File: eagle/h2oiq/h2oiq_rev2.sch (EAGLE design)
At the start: 25 parts, among them T1 Darlington, T2 BC846

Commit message: Minor board change for the LPFK
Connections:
- net SERVOON: now also ATMEL.PD2(INT0/PCINT18)
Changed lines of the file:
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@@
 <label x="33.02" y="27.94" size="1.778" layer="95"/>
+</segment>
+<segment>
+<pinref part="ATMEL" gate="1" pin="PD2(INT0/PCINT18)"/>
+<wire x1="25.4" y1="83.82" x2="30.48" y2="83.82" width="0.1524" layer="91"/>
+<label x="33.02" y="83.82" size="1.778" layer="95"/>
 </segment>
 </net>

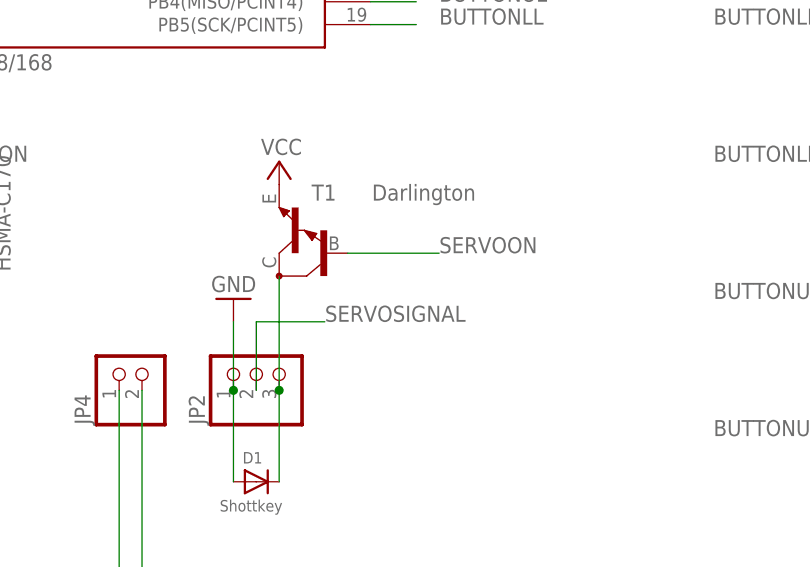
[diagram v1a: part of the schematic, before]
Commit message: Adding Demo Arduino Code, as well as updated board changes
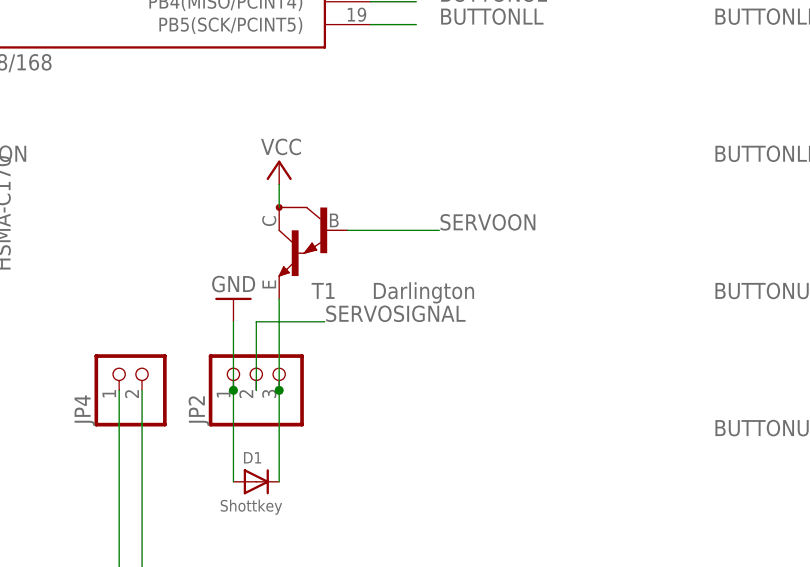
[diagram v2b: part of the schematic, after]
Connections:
- net SERVOACT: now also T1.E; no longer T1.C
- net VCC: now also T1.C; no longer T1.E
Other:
- moved on the sheet: T1
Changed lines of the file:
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@@
 <attribute name="VALUE" x="8.636" y="0.508" size="1.27" layer="96" rot="MR180"/>
 </instance>
-<instance part="T1" gate="G$1" x="20.32" y="27.94" smashed="yes" rot="R180">
-<attribute name="NAME" x="21.59" y="35.56" size="1.778" layer="95" rot="R180"/>
-<attribute name="VALUE" x="37.084" y="35.56" size="1.778" layer="96" rot="R180"/>
+<instance part="T1" gate="G$1" x="20.32" y="30.48" smashed="yes" rot="MR0">
+<attribute name="NAME" x="21.59" y="22.86" size="1.778" layer="95" rot="MR0"/>
+<attribute name="VALUE" x="37.084" y="22.86" size="1.778" layer="96" rot="MR0"/>
 </instance>
 <instance part="LED1" gate="G$1" x="-20.32" y="25.4"/>
@@
 </segment>
 <segment>
-<pinref part="P+6" gate="VCC" pin="VCC"/>
-<pinref part="T1" gate="G$1" pin="E"/>
-</segment>
-<segment>
 <pinref part="XBEE" gate="G$1" pin="VCC"/>
 <pinref part="P+3" gate="VCC" pin="VCC"/>
@@
 <label x="10.16" y="-15.24" size="1.778" layer="95"/>
 <pinref part="JP4" gate="G$1" pin="2"/>
+</segment>
+<segment>
+<pinref part="T1" gate="G$1" pin="C"/>
+<pinref part="P+6" gate="VCC" pin="VCC"/>
+<wire x1="15.24" y1="33.02" x2="15.24" y2="35.56" width="0.1524" layer="91"/>
 </segment>
 </net>
@@
 <net name="SERVOACT" class="0">
 <segment>
-<pinref part="T1" gate="G$1" pin="C"/>
-<wire x1="15.24" y1="12.7" x2="15.24" y2="25.4" width="0.1524" layer="91"/>
 <pinref part="JP2" gate="A" pin="3"/>
 <pinref part="D1" gate="G$1" pin="C"/>
 <wire x1="15.24" y1="2.54" x2="15.24" y2="12.7" width="0.1524" layer="91"/>
+<pinref part="T1" gate="G$1" pin="E"/>
+<wire x1="15.24" y1="22.86" x2="15.24" y2="12.7" width="0.1524" layer="91"/>
 <junction x="15.24" y="12.7"/>
 </segment>
@@
 <segment>
 <pinref part="T1" gate="G$1" pin="B"/>
-<wire x1="22.86" y1="27.94" x2="33.02" y2="27.94" width="0.1524" layer="91"/>
-<label x="33.02" y="27.94" size="1.778" layer="95"/>
-</segment>
-<segment>
+<wire x1="22.86" y1="30.48" x2="33.02" y2="30.48" width="0.1524" layer="91"/>
+<label x="33.02" y="30.48" size="1.778" layer="95"/>
+</segment>
+<segment>
